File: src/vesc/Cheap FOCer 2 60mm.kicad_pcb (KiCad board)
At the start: 6 copper layers, 72.8 x 100 mm, 158 parts, among them J1 Conn_01x02, J101 USB_C_Receptacle_USB2.0_16P, J2 Conn_01x03, J3 Conn_01x02, J7 Conn_02x03_Odd_Even, P4 HALL/Encoder, Q1 NCEP60T20, Q2 NCEP60T20, Q3 NCEP60T20, Q4 NCEP60T20, Q5 NCEP60T20, Q6 NCEP60T20, U1 HX4002, U2 DRV8301, U3 TCAN1462V, U3A1 TP2604-SR, U3B1 TP2604-SR, U3C1 TP2604-SR, U5 STM32F405RGT6, X1 24MHz

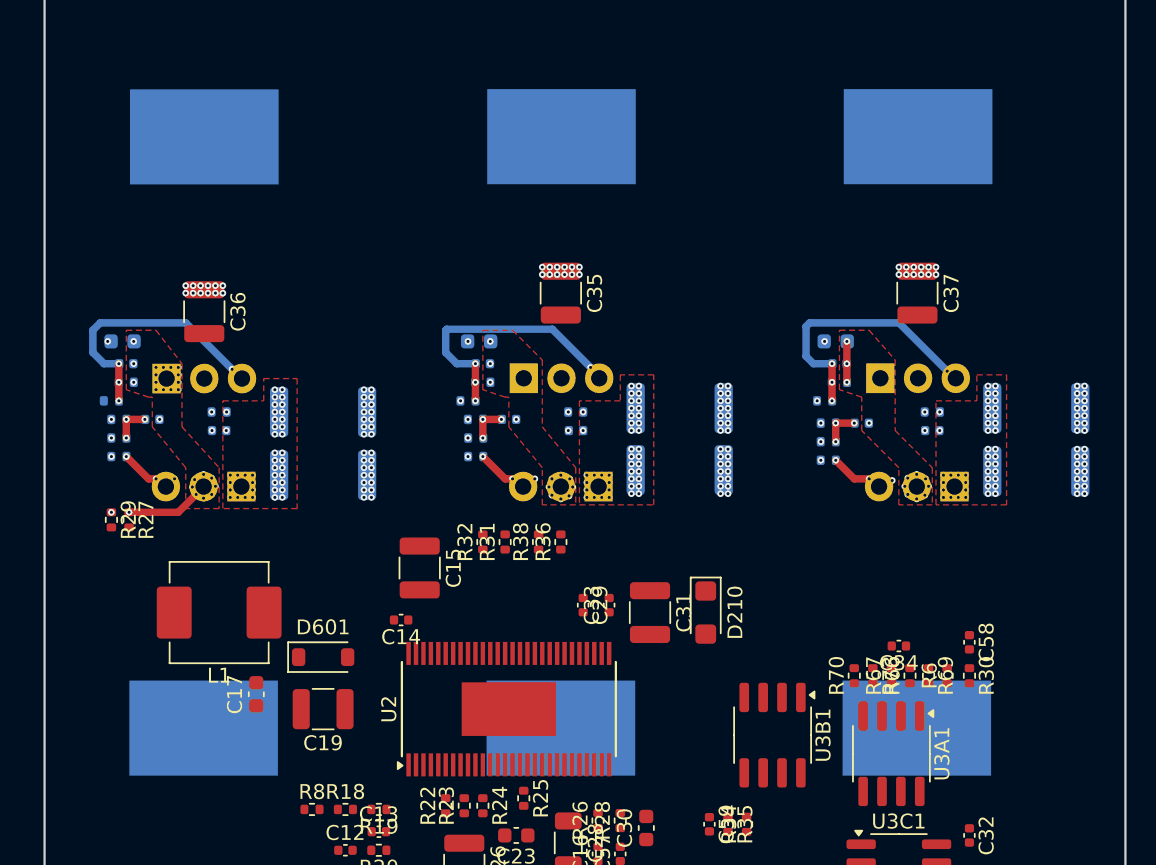
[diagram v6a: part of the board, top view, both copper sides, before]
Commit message: MOSFET positioning
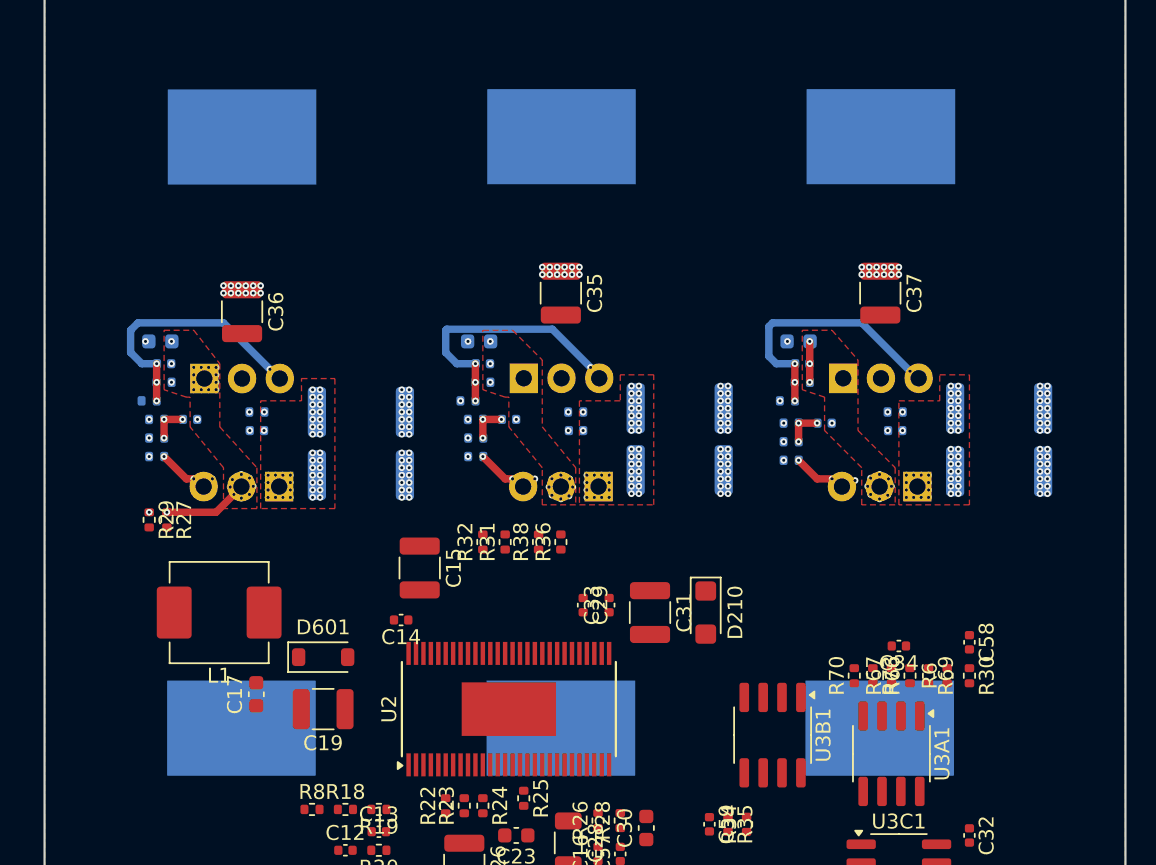
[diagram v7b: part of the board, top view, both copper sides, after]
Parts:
- moved C18 2.54 mm to (115.0, 77.8)
- moved C36 2.54 mm to (120.5, 75.8)
- moved C40 2.54 mm to (117.0, 83.0)
- moved C61 2.54 mm to (115.3, 79.2)
- moved C62 2.54 mm to (121.5, 83.8)
- moved Q1 2.54 mm to (115.4, 66.1)
- moved Q4 2.54 mm to (125.6, 101.7)
- moved R27 2.54 mm to (115.5, 89.8)
- moved R29 2.54 mm to (114.3, 89.8)
- moved R33 2.54 mm to (114.8, 83.0)
- moved R41 2.54 mm to (114.3, 81.8)
- moved R44 2.54 mm to (115.3, 80.5)
- moved R47 2.54 mm to (114.8, 85.5)
- moved R50 2.54 mm to (121.5, 82.5)
- moved R53 2.54 mm to (114.8, 84.2)
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
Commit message: giant capacitors
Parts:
- moved C39 146.7 mm to (153.8, 68.5), turned to 90 degrees
- moved C38 121.7 mm to (130.2, 68.5), turned to 90 degrees
- moved C18 2.00 mm to (113.0, 77.8)
- moved C27 2.00 mm to (160.0, 77.8)
- moved C36 2.00 mm to (118.5, 75.8)
- moved C37 2.00 mm to (165.5, 74.5)
- moved C40 2.00 mm to (115.0, 83.0)
- moved C42 2.00 mm to (161.8, 83.2)
- moved C61 2.00 mm to (113.3, 79.2)
- moved C62 2.00 mm to (119.5, 83.8)
- moved C66 2.00 mm to (160.2, 79.2)
- moved C67 2.00 mm to (166.5, 83.8)
- moved Q1 2.00 mm to (113.4, 66.1)
- moved Q3 2.00 mm to (160.4, 66.1)
- moved Q4 2.00 mm to (123.6, 101.7)
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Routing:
- net VCC: track 0.00 -> 13.0 mm, vias 0 -> 9
- net GND: track 0.00 -> 9.12 mm, vias 127 -> 226
- net /MCU/ADC_TEMP: track 0.00 -> 8.45 mm
- net Net-(U5-PH0-OSC_IN): track 0.00 -> 6.05 mm
- net Net-(U5-PH1-OSC_OUT): track 0.00 -> 5.28 mm
- net Net-(U5-VCAP1): track 0.00 -> 3.68 mm
- net Net-(U5-VCAP2): track 0.00 -> 2.68 mm, vias 0 -> 1
- net NRST: track 0.00 -> 2.64 mm
- net V_SUPPLY: vias 0 -> 81
- added copper zone on In2.Cu, net VCC
